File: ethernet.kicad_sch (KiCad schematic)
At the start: 39 parts, among them J1001 7499010121A, U1001 LAN8742A-CZ-TR, U1002 USBLC6-4SC6

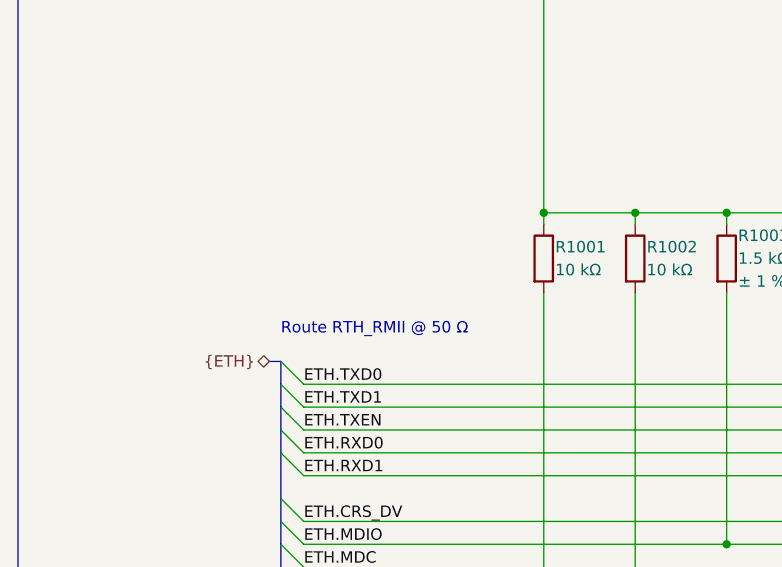
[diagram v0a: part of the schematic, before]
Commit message: Update ETH signal layout comments
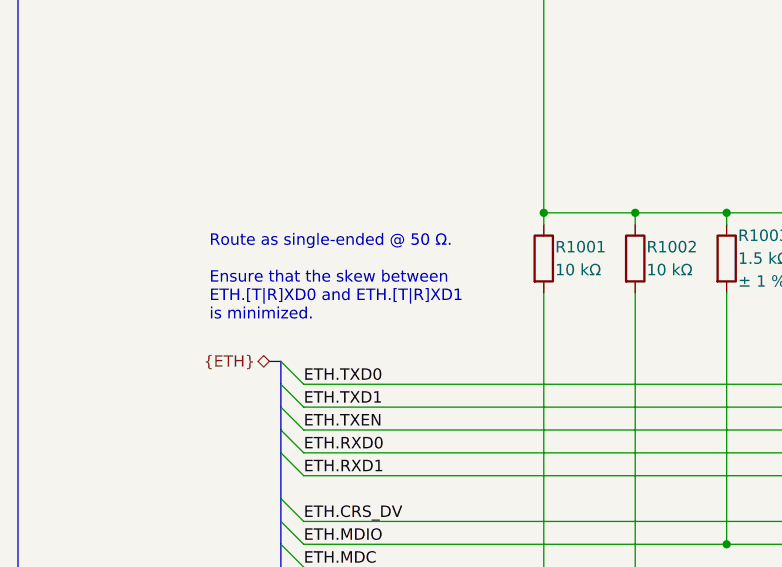
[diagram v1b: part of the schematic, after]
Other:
- note removed: "Route RTH_RMII @ 50 Ω"
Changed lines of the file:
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@@
-		)
-	)
-	(text "Route RTH_RMII @ 50 Ω"
-		(exclude_from_sim no)
-		(at 62.738 164.084 0)
-		(effects
-			(font
-				(size 1.27 1.27)
-				(color 194 0 194 1)
-			)
-			(justify right)
 		)
 	)
@@
 		)
 	)
+	(text_box "Route as single-ended @ 50 Ω.\n\nEnsure that the skew between ETH.[T|R]XD0 and ETH.[T|R]XD1 is minimized."
+		(exclude_from_sim no)
+		(at 33.02 152.4 0)
+		(size 34.29 12.7)
+		(margins 0.9525 0.9525 0.9525 0.9525)
+		(stroke
+			(width -0.0001)
+			(type solid)
+		)
+		(fill
+			(type none)
+		)
+		(effects
+			(font
+				(size 1.27 1.27)
+				(color 194 0 194 1)
+			)
+			(justify left top)
+		)
+	)

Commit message: Add additional info to passives
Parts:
- C1001: Size (none) -> 0805; Temperature coefficient (none) -> X5R; Tolerance (none) -> 20 %; Voltage rating ≥ 16 V -> 16 V
- C1002, C1003, C1004, C1005, C1007, C1008: Size (none) -> 0402; Temperature coefficient (none) -> X5R; Tolerance (none) -> 20 %; Voltage rating ≥ 16 V -> 16 V
- C1006: Size (none) -> 0402; Temperature coefficient (none) -> C0G; Tolerance (none) -> 2 %; Voltage rating ≥ 16 V -> 50 V
- R1001, R1002, R1004, R1005, R1006, R1010, R1011, R1012, R1016, R1018: MPN 560112110020 -> (none); Manufacturer Würth Elektronik -> (none); Power rating (none) -> 0.1 W; Size (none) -> 0402; Tolerance (none) -> 1 %
- R1003, R1019, R1020, R1021, R1022, R1023: Power rating (none) -> 0.1 W; Size (none) -> 0402; Tolerance ± 1 % -> 1 %
- R1007, R1008, R1009, R1013, R1014, R1015, R1017: footprint perfect_footprints:R_0402_1005Metric -> (none); MPN 560112110020 -> (none); Manufacturer Würth Elektronik -> (none); Size (none) -> 0402
- R1024, R1025: MPN 560112110019 -> (none); Manufacturer Würth Elektronik -> (none); Power rating (none) -> 0.1 W; Size (none) -> 0402; Tolerance (none) -> 1 %
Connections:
- net CLKIN: now also R1017.2; no longer R1017.1
- net ETH.CRS_DV: now also R1012.1; no longer R1012.2
- net ETH.INT_N: now also R1016.1; no longer R1016.2
- net ETH.MDC: now also R1014.1; no longer R1014.2
- net ETH.MDIO: now also R1013.1; no longer R1013.2
- net ETH.REF_CLK: now also R1017.1; no longer R1017.2
- net ETH.RST_N: now also R1015.1; no longer R1015.2
- net ETH.RXD0: now also R1010.1; no longer R1010.2
- net ETH.RXD1: now also R1011.1; no longer R1011.2
- net ETH.TXD0: now also R1007.1; no longer R1007.2
- net ETH.TXD1: now also R1008.1; no longer R1008.2
- net ETH.TXEN: now also R1009.1; no longer R1009.2
- net INT_N: now also R1016.2; no longer R1016.1
- net MDC: now also R1014.2; no longer R1014.1
- net MDIO: now also R1013.2; no longer R1013.1
- net MODE0: now also R1012.2; no longer R1012.1
- net RST_N: now also R1015.2; no longer R1015.1
- net RXD0: now also R1010.2; no longer R1010.1
- net RXD1: now also R1011.2; no longer R1011.1
- net TXD0: now also R1007.2; no longer R1007.1
- net TXD1: now also R1008.2; no longer R1008.1
- net TXEN: now also R1009.2; no longer R1009.1
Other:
- moved on the sheet: FB1001, J1001, TP1001, TP1002, U1001, U1002

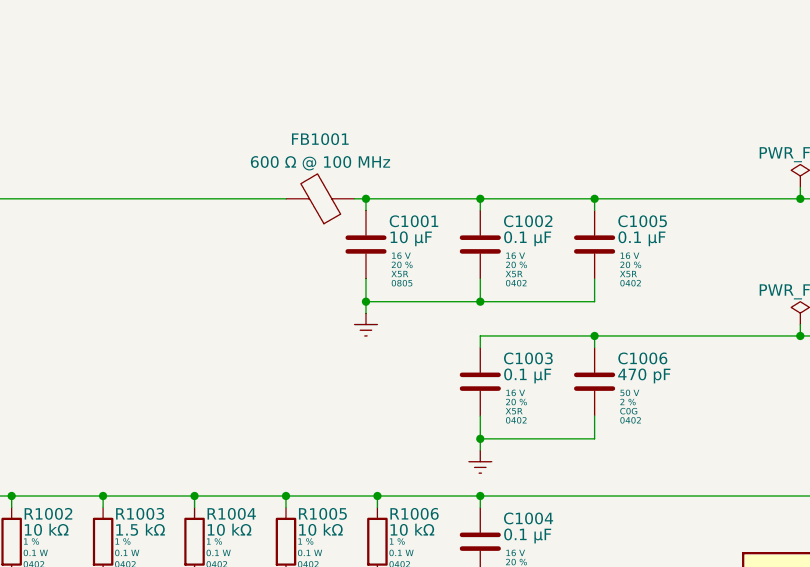
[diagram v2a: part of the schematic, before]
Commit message: Update capacitor BOM
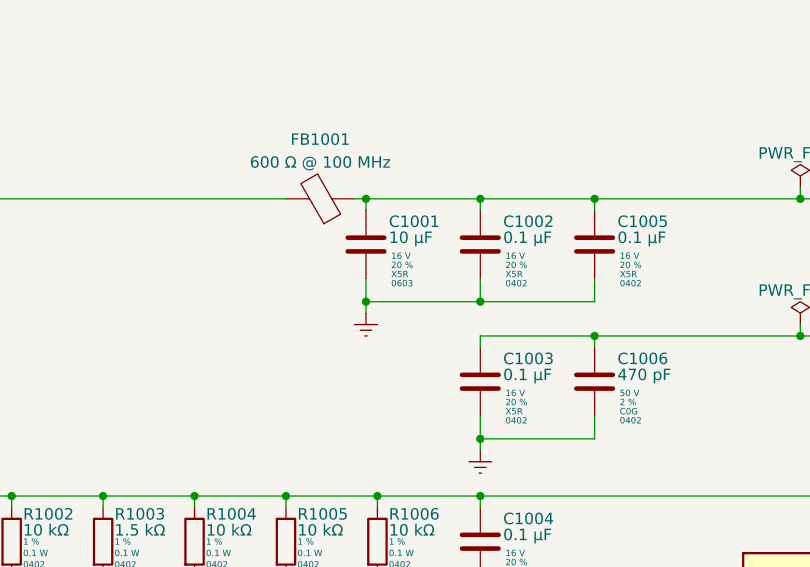
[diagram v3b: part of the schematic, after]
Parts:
- C1001: footprint (none) -> Capacitor_SMD:C_0603_1608Metric; Digi-Key Part Number (none) -> 490-13248-1-ND; MPN (none) -> GRM188R6YA106MA73D; Manufacturer (none) -> Murata Electronics; Size 0805 -> 0603
- C1002, C1003, C1004, C1005, C1007, C1008: footprint (none) -> perfect_footprints:C_0402_1005Metric; Digi-Key Part Number (none) -> 490-10700-1-ND; MPN (none) -> GRM155R71H104KE14D; Manufacturer (none) -> Murata Electronics
- C1006: footprint (none) -> perfect_footprints:C_0402_1005Metric; Digi-Key Part Number (none) -> 490-1297-1-ND; MPN (none) -> GRM1555C1H471JA01D; Manufacturer (none) -> Murata Electronics
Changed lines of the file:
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@@
 			)
 		)
-		(property "Footprint" ""
+		(property "Footprint" "perfect_footprints:C_0402_1005Metric"
 			(at 171.1452 142.24 0)
 			(effects
@@
 			)
 		)
-		(property "Datasheet" ""
+		(property "Datasheet" "https://search.murata.co.jp/Ceramy/image/img/A01X/G101/ENG/GRM155R71H104KE14-01.pdf"
 			(at 170.18 138.43 0)
 			(effects
@@
 			)
 		)
-		(property "Description" ""
+		(property "Description" "0.1 µF ±10% 50V Ceramic Capacitor X7R 0402 (1005 Metric)"
 			(at 170.18 138.43 0)
 			(effects
@@
 			)
 		)
-		(property "MPN" ""
+		(property "MPN" "GRM155R71H104KE14D"
 			(at 170.18 138.43 0)
 			(effects
@@
 			)
 		)
-		(property "Manufacturer" ""
+		(property "Manufacturer" "Murata Electronics"
 			(at 170.18 138.43 0)
 			(effects
@@
 			)
 		)
+		(property "Digi-Key Part Number" "490-10700-1-ND"
+			(at 170.18 138.43 0)
+			(effects
+				(font
+					(size 1.27 1.27)
+				)
+				(hide yes)
+			)
+		)
 		(pin "2"
 		)
@@
 			)
 		)
-		(property "Footprint" ""
+		(property "Footprint" "Capacitor_SMD:C_0603_1608Metric"
 			(at 158.4452 127 0)
 			(effects
@@
 			)
 		)
-		(property "Datasheet" ""
+		(property "Datasheet" "https://search.murata.co.jp/Ceramy/image/img/A01X/G101/ENG/GRM188R6YA106MA73-01A.pdf"
 			(at 157.48 123.19 0)
 			(effects
@@
 			)
 		)
-		(property "Description" ""
+		(property "Description" "10 µF ±20% 35V Ceramic Capacitor X5R 0603 (1608 Metric)"
 			(at 157.48 123.19 0)
 			(effects
@@
 			)
 		)
-		(property "MPN" ""
+		(property "MPN" "GRM188R6YA106MA73D"
 			(at 157.48 123.19 0)
 			(effects
@@
 			)
 		)
-		(property "Manufacturer" ""
+		(property "Manufacturer" "Murata Electronics"
 			(at 157.48 123.19 0)
 			(effects
@@
 			)
 		)
-		(property "Size" "0805"
+		(property "Size" "0603"
 			(at 160.274 127.508 0)
 			(effects
@@
 			)
 		)
+		(property "Digi-Key Part Number" "490-13248-1-ND"
+			(at 157.48 123.19 0)
+			(effects
+				(font
+					(size 1.27 1.27)
+				)
+				(hide yes)
+			)
+		)
 		(pin "2"
 		)
@@
 			)
 		)
-		(property "Footprint" ""
+		(property "Footprint" "perfect_footprints:C_0402_1005Metric"
 			(at 183.8452 142.24 0)
 			(effects
@@
 			)
 		)
-		(property "Datasheet" ""
+		(property "Datasheet" "https://search.murata.co.jp/Ceramy/image/img/A01X/G101/ENG/GRM1555C1H471JA01-01.pdf"
 			(at 182.88 138.43 0)
 			(effects
@@
 			)
 		)
-		(property "Description" ""
+		(property "Description" "470 pF ±5% 50V Ceramic Capacitor C0G, NP0 0402 (1005 Metric)"
 			(at 182.88 138.43 0)
 			(effects
@@
 			)
 		)
-		(property "MPN" ""
+		(property "MPN" "GRM1555C1H471JA01D"
 			(at 182.88 138.43 0)
 			(effects
@@
 			)
 		)
-		(property "Manufacturer" ""
+		(property "Manufacturer" "Murata Electronics"
 			(at 182.88 138.43 0)
 			(effects
@@
 			)
 		)
+		(property "Digi-Key Part Number" "490-1297-1-ND"
+			(at 182.88 138.43 0)
+			(effects
+				(font
+					(size 1.27 1.27)
+				)
+				(hide yes)
+			)
+		)
 		(pin "2"
 		)
@@
 			)
 		)
-		(property "Footprint" ""
+		(property "Footprint" "perfect_footprints:C_0402_1005Metric"
 			(at 171.1452 127 0)
 			(effects
@@
 			)
 		)
-		(property "Datasheet" ""
+		(property "Datasheet" "https://search.murata.co.jp/Ceramy/image/img/A01X/G101/ENG/GRM155R71H104KE14-01.pdf"
 			(at 170.18 123.19 0)
 			(effects
@@
 			)
 		)
-		(property "Description" ""
+		(property "Description" "0.1 µF ±10% 50V Ceramic Capacitor X7R 0402 (1005 Metric)"
 			(at 170.18 123.19 0)
 			(effects
@@
 			)
 		)
-		(property "MPN" ""
+		(property "MPN" "GRM155R71H104KE14D"
 			(at 170.18 123.19 0)
 			(effects
@@
 			)
 		)
-		(property "Manufacturer" ""
+		(property "Manufacturer" "Murata Electronics"
 			(at 170.18 123.19 0)
 			(effects
@@
 			)
 		)
+		(property "Digi-Key Part Number" "490-10700-1-ND"
+			(at 170.18 123.19 0)
+			(effects
+				(font
+					(size 1.27 1.27)
+				)
+				(hide yes)
+			)
+		)
 		(pin "2"
 		)
@@
 			)
 		)
-		(property "Footprint" ""
+		(property "Footprint" "perfect_footprints:C_0402_1005Metric"
 			(at 171.1452 160.02 0)
 			(effects
@@
 			)
 		)
-		(property "Datasheet" ""
+		(property "Datasheet" "https://search.murata.co.jp/Ceramy/image/img/A01X/G101/ENG/GRM155R71H104KE14-01.pdf"
 			(at 170.18 156.21 0)
 			(effects
@@
 			)
 		)
-		(property "Description" ""
+		(property "Description" "0.1 µF ±10% 50V Ceramic Capacitor X7R 0402 (1005 Metric)"
 			(at 170.18 156.21 0)
 			(effects
@@
 			)
 		)
-		(property "MPN" ""
+		(property "MPN" "GRM155R71H104KE14D"
 			(at 170.18 156.21 0)
 			(effects
@@
 			)
 		)
-		(property "Manufacturer" ""
+		(property "Manufacturer" "Murata Electronics"
 			(at 170.18 156.21 0)
 			(effects
@@
 			)
 		)
+		(property "Digi-Key Part Number" "490-10700-1-ND"
+			(at 170.18 156.21 0)
+			(effects
+				(font
+					(size 1.27 1.27)
+				)
+				(hide yes)
+			)
+		)
 		(pin "2"
 		)
@@
 			)
 		)
-		(property "Footprint" ""
+		(property "Footprint" "perfect_footprints:C_0402_1005Metric"
 			(at 337.5152 217.17 0)
 			(effects
@@
 			)
 		)
-		(property "Datasheet" ""
+		(property "Datasheet" "https://search.murata.co.jp/Ceramy/image/img/A01X/G101/ENG/GRM155R71H104KE14-01.pdf"
 			(at 336.55 213.36 0)
 			(effects
@@
 			)
 		)
-		(property "Description" ""
+		(property "Description" "0.1 µF ±10% 50V Ceramic Capacitor X7R 0402 (1005 Metric)"
 			(at 336.55 213.36 0)
 			(effects
@@
 			)
 		)
-		(property "MPN" ""
+		(property "MPN" "GRM155R71H104KE14D"
 			(at 336.55 213.36 0)
 			(effects
@@
 			)
 		)
-		(property "Manufacturer" ""
+		(property "Manufacturer" "Murata Electronics"
 			(at 336.55 213.36 0)
 			(effects
@@
 			)
 		)
+		(property "Digi-Key Part Number" "490-10700-1-ND"
+			(at 336.55 213.36 0)
+			(effects
+				(font
+					(size 1.27 1.27)
+				)
+				(hide yes)
+			)
+		)
 		(pin "2"
 		)
@@
 			)
 		)
-		(property "Footprint" ""
+		(property "Footprint" "perfect_footprints:C_0402_1005Metric"
 			(at 183.8452 127 0)
 			(effects
@@
 			)
 		)
-		(property "Datasheet" ""
+		(property "Datasheet" "https://search.murata.co.jp/Ceramy/image/img/A01X/G101/ENG/GRM155R71H104KE14-01.pdf"
 			(at 182.88 123.19 0)
 			(effects
@@
 			)
 		)
-		(property "Description" ""
+		(property "Description" "0.1 µF ±10% 50V Ceramic Capacitor X7R 0402 (1005 Metric)"
 			(at 182.88 123.19 0)
 			(effects
@@
 			)
 		)
-		(property "MPN" ""
+		(property "MPN" "GRM155R71H104KE14D"
 			(at 182.88 123.19 0)
 			(effects
@@
 			)
 		)
-		(property "Manufacturer" ""
+		(property "Manufacturer" "Murata Electronics"
 			(at 182.88 123.19 0)
 			(effects
@@
 			)
 		)
+		(property "Digi-Key Part Number" "490-10700-1-ND"
+			(at 182.88 123.19 0)
+			(effects
+				(font
+					(size 1.27 1.27)
+				)
+				(hide yes)
+			)
+		)
 		(pin "2"
 		)
@@
 			)
 		)
-		(property "Footprint" ""
+		(property "Footprint" "perfect_footprints:C_0402_1005Metric"
 			(at 327.9648 217.17 0)
 			(effects
@@
 			)
 		)
-		(property "Datasheet" ""
+		(property "Datasheet" "https://search.murata.co.jp/Ceramy/image/img/A01X/G101/ENG/GRM155R71H104KE14-01.pdf"
 			(at 328.93 213.36 0)
 			(effects
@@
 			)
 		)
-		(property "Description" ""
+		(property "Description" "0.1 µF ±10% 50V Ceramic Capacitor X7R 0402 (1005 Metric)"
 			(at 328.93 213.36 0)
 			(effects
@@
 			)
 		)
-		(property "MPN" ""
+		(property "MPN" "GRM155R71H104KE14D"
 			(at 328.93 213.36 0)
 			(effects
@@
 			)
 		)
-		(property "Manufacturer" ""
+		(property "Manufacturer" "Murata Electronics"
 			(at 328.93 213.36 0)
 			(effects
@@
 			)
 		)
+		(property "Digi-Key Part Number" "490-10700-1-ND"
+			(at 328.93 213.36 0)
+			(effects
+				(font
+					(size 1.27 1.27)
+				)
+				(hide yes)
+			)
+		)

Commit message: Update R & L BOM
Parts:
- R1001, R1002, R1004, R1005, R1006, R1018: Digi-Key Part Number (none) -> P10.0KLCT-ND; MPN (none) -> ERJ-2RKF1002X; Manufacturer (none) -> Panasonic Electronic Components
- R1003: Digi-Key Part Number (none) -> P1.50KLCT-ND; MPN (none) -> ERJ-2RKF1501X; Manufacturer (none) -> Panasonic Electronic Components
- R1007, R1008, R1009, R1013, R1014, R1015, R1017: footprint (none) -> perfect_footprints:R_0402_1005Metric; Digi-Key Part Number (none) -> P0.0JCT-ND; MPN (none) -> ERJ-2GE0R00X; Manufacturer (none) -> Panasonic Electronic Components
- R1010, R1011, R1012, R1016: Digi-Key Part Number (none) -> P33.0LCT-ND; MPN (none) -> ERJ-2RKF33R0X; Manufacturer (none) -> Panasonic Electronic Components
- R1019, R1021, R1022, R1023: Digi-Key Part Number (none) -> P49.9LCT-ND; MPN (none) -> ERJ-2RKF49R9X; Manufacturer (none) -> Panasonic Electronic Components
- R1020: Digi-Key Part Number (none) -> P12.1KLCT-ND; MPN (none) -> ERJ-2RKF1212X; Manufacturer (none) -> Panasonic Electronic Components
- R1024, R1025: Digi-Key Part Number (none) -> 732-560112110231CT-ND; MPN (none) -> 560112110231; Manufacturer (none) -> Würth Elektronik

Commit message: Fill BOM info
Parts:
- FB1001: footprint (none) -> Inductor_SMD:L_0603_1608Metric; Digi-Key Part Number (none) -> 445-MPZ1608S601ATA00CT-ND; MPN (none) -> MPZ1608S601ATA00; Manufacturer (none) -> TDK Corporation
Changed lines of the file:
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@@
 			)
 		)
-		(property "Footprint" ""
+		(property "Footprint" "Inductor_SMD:L_0603_1608Metric"
 			(at 152.4 119.888 90)
 			(effects
@@
 			)
 		)
-		(property "Datasheet" "~"
+		(property "Datasheet" "https://product.tdk.com/en/system/files?file=dam/doc/product/emc/emc/beads/catalog/beads_commercial_power_mpz1608_en.pdf"
 			(at 152.4 118.11 0)
 			(effects
@@
 			)
 		)
-		(property "Description" "Ferrite bead"
+		(property "Description" "600 Ohms @ 100 MHz 1 Power Line Ferrite Bead 0603 (1608 Metric) 1A 150mOhm"
 			(at 152.4 118.11 0)
 			(effects
 				(font
+					(size 1.27 1.27)
+				)
+				(hide yes)
+			)
+		)
+		(property "Digi-Key Part Number" "445-MPZ1608S601ATA00CT-ND"
+			(at 152.4 118.11 90)
+			(effects
+				(font
+					(size 1.27 1.27)
+				)
+				(hide yes)
+			)
+		)
+		(property "MPN" "MPZ1608S601ATA00"
+			(at 152.4 118.11 90)
+			(effects
+				(font
+					(size 1.27 1.27)
+				)
+				(hide yes)
+			)
+		)
+		(property "Manufacturer" "TDK Corporation"
+			(at 152.4 118.11 90)
+			(effects
+				(font
